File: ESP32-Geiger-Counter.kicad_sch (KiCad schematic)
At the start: 44 parts, among them J1 USB_C_Receptacle_USB2.0_16P, Q1 Q_NPN_BCE, Q2 Q_NPN_BCE, SW1 SW_Push, SW2 SW_Push, U1 TP4056-42-ESOP8, U2 USBLC6-2SC6, U3 ESP32-WROOM-32, U4 TPS63031DSK, U5 Geiger Mueller Tube, U6 CP2102N-Axx-xQFN24

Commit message: basically restarting
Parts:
- removed BT1: Battery_Cell, Connector_JST:JST_PH_B2B-PH-K_1x02_P2.00mm_Vertical, symbol Device:Battery_Cell
- removed C10, C11, C12, C14, C15, C6: 100nF, symbol Device:C
- removed C13, C7, C8: 10uF, symbol Device:C
- removed C16: 100uF, symbol Device:C
- removed C9: 22uF, symbol Device:C
- removed D1: Red LED, symbol Device:LED
- removed D2: Green LED, symbol Device:LED
- removed D3, D4: D_Schottky, symbol Device:D_Schottky
- removed J1: USB_C_Receptacle_USB2.0_16P, symbol Connector:USB_C_Receptacle_USB2.0_16P
- removed Q1, Q2: Q_NPN_BCE, symbol Transistor_BJT:Q_NPN_BCE
- removed R1, R2: 5.1K, symbol Device:R
- removed R10, R11, R5, R9: 10K, symbol Device:R
- removed R3: 22K, symbol Device:R
- removed R4: 2K, symbol Device:R
- removed R6, R7: 1K, symbol Device:R
- removed R8: 47K, symbol Device:R
- removed SW1, SW2: SW_Push, symbol Switch:SW_Push
- removed U1: TP4056-42-ESOP8, Package_SO:SOIC-8-1EP_3.9x4.9mm_P1.27mm_EP2.41x3.3mm_ThermalVias, symbol Battery_Management:TP4056-42-ESOP8
- removed U2: USBLC6-2SC6, Package_TO_SOT_SMD:SOT-23-6, symbol Power_Protection:USBLC6-2SC6
- removed U3: ESP32-WROOM-32, RF_Module:ESP32-WROOM-32, symbol RF_Module:ESP32-WROOM-32
- removed U4: TPS63031DSK, Package_SON:WSON-10-1EP_2.5x2.5mm_P0.5mm_EP1.2x2mm, symbol Regulator_Switching:TPS63031DSK
- removed U5: Geiger Mueller Tube, symbol Custom Parts:Geiger_Mueller_Tube
- removed U6: CP2102N-Axx-xQFN24, Package_DFN_QFN:QFN-24-1EP_4x4mm_P0.5mm_EP2.6x2.6mm, symbol Interface_USB:CP2102N-Axx-xQFN24
- added C1: 1uF, symbol Device:C
- added J1: 2s1p Lipo Battery Pack (8.4V-6V), symbol Connector_Generic:Conn_01x02
- added J2: USB_C_Receptacle_USB2.0_16P, Connector_USB:USB_C_Receptacle_GCT_USB4105-xx-A_16P_TopMnt_Horizontal, symbol Connector:USB_C_Receptacle_USB2.0_16P
- added R1, R2: 5.1K, symbol Device:R_US
- added U1: BQ25886RGE, Package_DFN_QFN:Texas_RGE0024H_VQFN-24-1EP_4x4mm_P0.5mm_EP2.7x2.7mm, symbol Battery_Management:BQ25886RGE
- C2: value 10uF -> 30uF
- C3: value 100nF -> 10uF
- C4: value 10uF -> 47nF
- C5: value 10uF -> 44uF
- F1: value Polyfuse 500mA -> 3A Polyfuse; footprint Fuse:Fuse_1812_4532Metric -> (none)
- L1: value 1.5uH -> 1uH
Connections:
- net +5V: now also F1.1, C1.2, U1.23 (VBUS); no longer C2.1, C3.1, F1.2
- net D+: now also J2.A6 (D+), J2.B6 (D+), U1.24 (D+)
- net D-: now also J2.A7 (D-), J2.B7 (D-), U1.1 (D-)
- net GND: now also C2.1, C3.1, C1.1, J1.1 (Pin_1), J2.A1 (GND), J2.A12 (GND), J2.B1 (GND), J2.B12 (GND), J2.SH (SHIELD), R1.2, R2.1; no longer C2.2, C3.2, C4.1
- net at L1.2: now also C4.1, U1.17 (SW), U1.18 (SW)
- net at L1.1: now also C2.2, C3.2, U1.21 (PMID), U1.22 (PMID)
- net VBAT: no longer names the net of C4.2
- net VBAT: now also U1.12 (BTST)
- net VPWR renamed SYS
- net SYS: now also U1.15 (SYS), U1.16 (SYS)
- new net: F1.2, J2.A4 (VBUS), J2.A9 (VBUS), J2.B4 (VBUS), J2.B9 (VBUS)
- new net: J2.A5 (CC1), R1.1
- new net: J2.B5 (CC2), R2.2
- new net: U1.13 (BAT), U1.14 (BAT)
- new net: U1.19 (GND), U1.20 (GND), U1.25 (GND), U1.4 (GND)
- new net BATT: J1.2 (Pin_2)
- no-connect marks 12 -> 2
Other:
- note added: "Battery Connector"
- note added: "USB Interface"
- note removed: "3.3V Buck Boost Converter"
- note removed: "3.7V Lipo Cell"
- note removed: "Boot/Reset stuff"
- note removed: "Lipo Charging"
- note removed: "Power OR Gate"
- note removed: "USB Input"
- note removed: "USB to ESP"

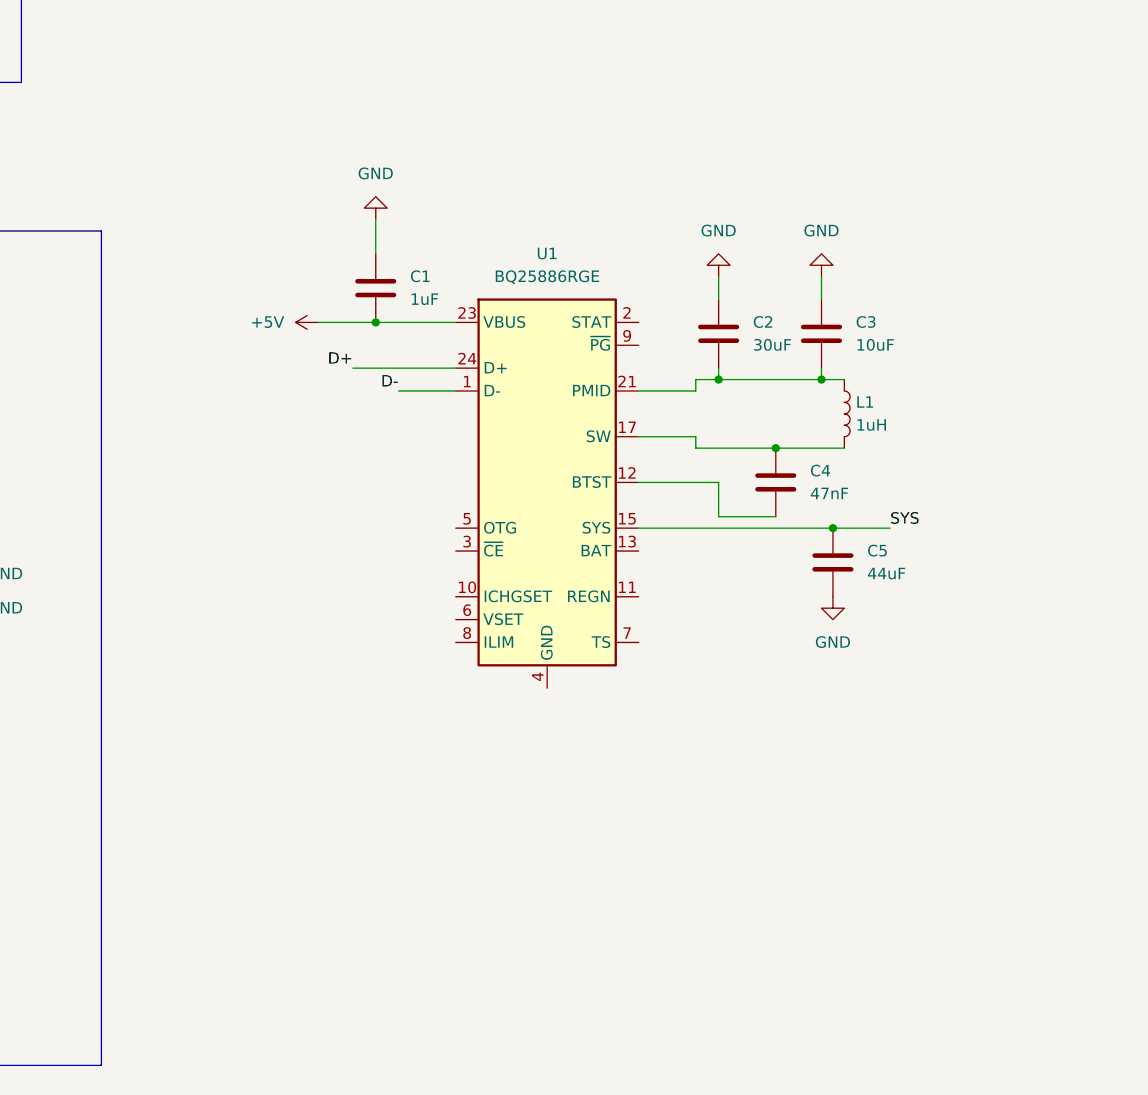
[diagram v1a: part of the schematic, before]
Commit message: added battery charging ic
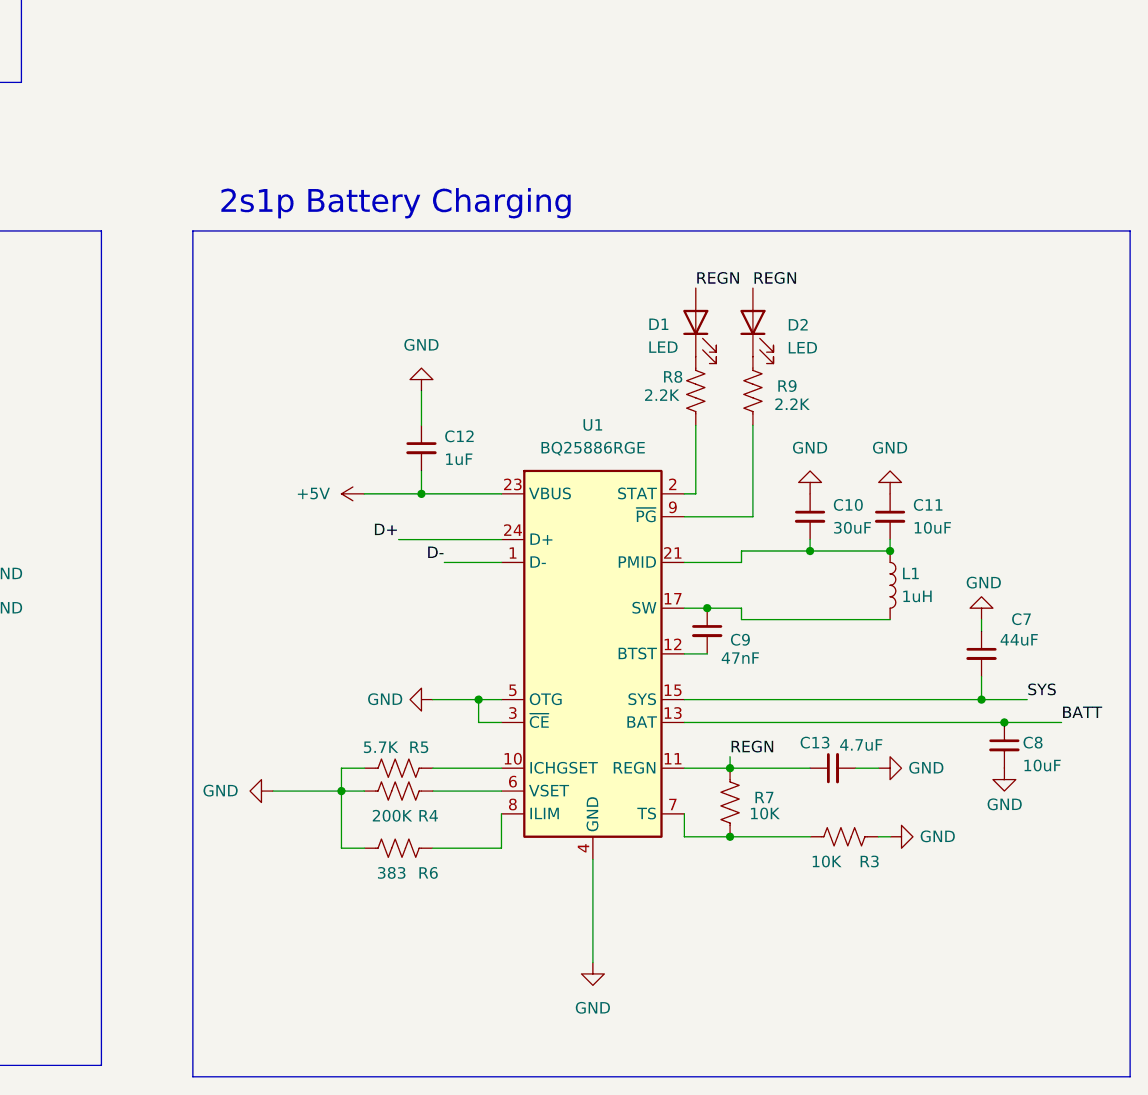
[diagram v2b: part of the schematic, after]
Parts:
- removed C1: 1uF, symbol Device:C
- removed C2: 30uF, symbol Device:C
- removed C3: 10uF, symbol Device:C
- removed C4: 47nF, symbol Device:C
- removed C5: 44uF, symbol Device:C
- added C10: 30uF, symbol Device:C_Small
- added C11, C8: 10uF, symbol Device:C_Small
- added C12: 1uF, symbol Device:C_Small
- added C13: 4.7uF, symbol Device:C_Small
- added C7: 44uF, symbol Device:C_Small
- added C9: 47nF, symbol Device:C_Small
- added D1, D2: LED, symbol Device:LED
- added R3, R7: 10K, symbol Device:R_US
- added R4: 200K, symbol Device:R_US
- added R5: 5.7K, symbol Device:R_US
- added R6: 383, symbol Device:R_US
- added R8, R9: 2.2K, symbol Device:R_US
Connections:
- net +5V: now also C12.2
- net BATT: now also U1.13 (BAT), U1.14 (BAT), C8.1
- net GND: now also U1.19 (GND), U1.20 (GND), U1.25 (GND), U1.3 (~{CE}), U1.4 (GND), U1.5 (OTG), C10.1, C11.1, C12.1, C13.2, C7.1, C8.2, R3.2, R4.1, R5.2, R6.1
- net SYS: now also C7.2
- net at L1.1, U1.21 (PMID), U1.22 (PMID): now also C10.2, C11.2
- net at L1.2, U1.17 (SW), U1.18 (SW): now also C9.1
- net at U1.12 (BTST): now also C9.2
- net at U1.10 (ICHGSET): now also R5.1
- net REGN: now reaches U1.11 (REGN)
- net REGN: now also C13.1, D1.2 (A), D2.2 (A), R7.2
- net at U1.2 (STAT): now also R8.1
- net at U1.6 (VSET): now also R4.2
- net at U1.7 (TS): now also R3.1, R7.1
- net at U1.8 (ILIM): now also R6.2
- net at U1.9 (~{PG}): now also R9.1
- new net: D2.1 (K), R9.2
- new net: D1.1 (K), R8.2
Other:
- note added: "2s1p Battery Charging"
- moved on the sheet: L1, U1

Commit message: big changes, added esp32 wroom 1
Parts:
- added C14, C18, C20: 100nF, symbol Device:C_Small
- added C15, C19: 10uF, symbol Device:C_Small
- added C16, C17: 22uF, symbol Device:C_Small
- added C21: 47uF, symbol Device:C_Small
- added C22: 1uF, symbol Device:C_Small
- added L2: 3.9uH, symbol Device:L
- added R10: 1M, symbol Device:R_US
- added R11: 330k, symbol Device:R_US
- added R12, R13: 10K, symbol Device:R_US
- added SW1: SW_SPDT, symbol Switch:SW_SPDT
- added SW2: RESET, symbol Switch:SW_Push
- added SW3: BOOT, symbol Switch:SW_Push
- added U2: AP63203WU, Package_TO_SOT_SMD:TSOT-23-6, symbol Regulator_Switching:AP63203WU
- added U3: ESP32-S3-WROOM-1, RF_Module:ESP32-S3-WROOM-1, symbol RF_Module:ESP32-S3-WROOM-1
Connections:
- net D+: now also U3.14 (USB_D+)
- net D-: now also U3.13 (USB_D-)
- net GND: now also C15.2, C16.2, C17.2, C18.2, C19.2, C20.2, C21.2, C22.2, R11.1, SW2.2, SW3.1, U2.4 (GND), U3.1 (GND), U3.40 (GND), U3.41 (GND)
- net SYS: now also SW1.2 (B)
- new net: R13.2, SW3.2, U3.27 (IO0)
- new net: C22.1, R12.1, SW2.1, U3.3 (EN)
- new net: C14.1, L2.1, U2.5 (SW)
- new net: C14.2, U2.6 (BST)
- new net +3.3V: C16.1, C17.1, C19.1, C20.1, C21.1, L2.2, R12.2, R13.1, U2.1 (FB), U3.2 (3V3)
- new net VBAT_SENSE: C18.1, R10.1, R11.2
- new net VSYS_SW: C15.1, R10.2, SW1.1 (A), U2.2 (EN), U2.3 (IN)
- no-connect marks 2 -> 3
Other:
- note added: "3.3V Buck Converter"
- note added: "Battery Voltage to ESP32"
- note added: "Main on/off switch"

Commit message: working on HV boost
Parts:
- added C23: 10uF 25V, symbol Device:C_Small
- added C24, C25, C27: 10nF 1kV, symbol Device:C_Small
- added C26: 10nF, symbol Device:C_Small
- added D3: 1000V, symbol Device:D
- added D4, D5, D6: 150V Zener, symbol Device:D_Zener
- added J3: SBM20 +, symbol Connector_Generic:Conn_01x01
- added J4: SBM20 -, symbol Connector_Generic:Conn_01x01
- added L3: 10mH, symbol Device:L
- added Q1: NMOS, symbol Simulation_SPICE:NMOS
- added Q2: 2N3904, Package_TO_SOT_THT:TO-92_Inline, symbol Transistor_BJT:2N3904
- added R14, R15, R16: 100M, symbol Device:R_US
- added R17: 680k, symbol Device:R_US
- added R18: 1M, symbol Device:R_US
- added R19: 5.1M, symbol Device:R_US
- added R20: 100k, symbol Device:R_US
- added R21, R22: 10k, symbol Device:R_US
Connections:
- net +3.3V: now also R22.1
- net GND: now also C23.2, C24.2, C25.2, C26.2, C27.2, D6.2 (A), Q1.3 (S), Q2.1 (E), R17.1, R20.1
- net VSYS_SW: now also C23.1, L3.1
- new net: J4.1 (Pin_1), R20.2, R21.1
- new net: C24.1, C25.1, D3.1 (K), D4.1 (K), R14.2, R18.1
- new net: D3.2 (A), L3.2, Q1.1 (D)
- new net: R15.1, R16.2
- new net: R14.1, R15.2
- new net: D4.2 (A), D5.1 (K)
- new net: D5.2 (A), D6.1 (K)
- new net: C27.1, R18.2, R19.1
- new net: J3.1 (Pin_1), R19.2
- new net: Q2.2 (B), R21.2
- new net HV_SENSE: C26.1, R16.1, R17.2
- new net PULSE: Q2.3 (C), R22.2

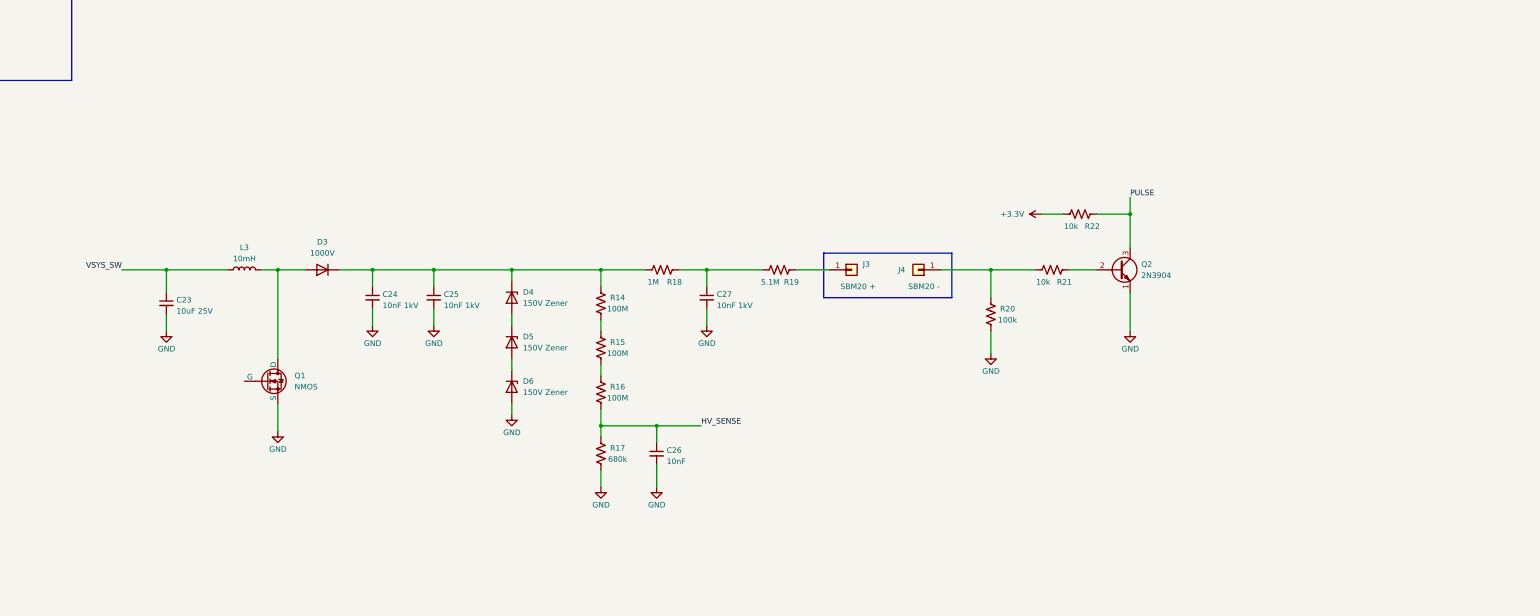
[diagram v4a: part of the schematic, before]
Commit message: finished working 400v boost and tube topo
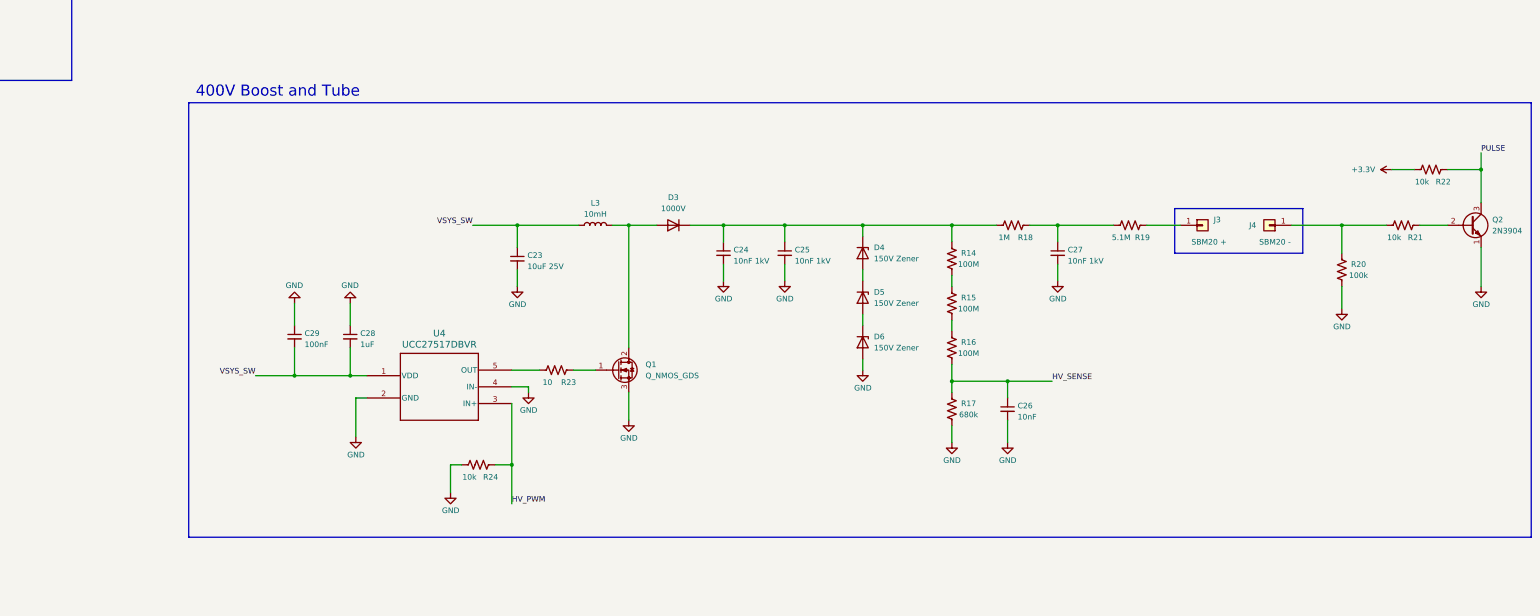
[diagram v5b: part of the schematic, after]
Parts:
- removed Q1: NMOS, symbol Simulation_SPICE:NMOS
- added C28: 1uF, symbol Device:C_Small
- added C29: 100nF, symbol Device:C_Small
- added Q1: Q_NMOS_GDS, Package_TO_SOT_SMD:SOT-223-3_TabPin2, symbol Transistor_FET:Q_NMOS_GDS
- added R23: 10, symbol Device:R_US
- added R24: 10k, symbol Device:R_US
- added U4: UCC27517DBVR, footprints:DBV5_TEX, symbol UCC27517:UCC27517DBVR
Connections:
- net GND: now also C28.1, C29.1, Q1.3 (S), R24.1, U4.2 (GND), U4.4 (IN-)
- net VSYS_SW: now also C28.2, C29.2, U4.1 (VDD)
- net at D3.2 (A), L3.2: now also Q1.2 (D)
- new net: Q1.1 (G), R23.2
- new net: R23.1, U4.5 (OUT)
- new net HV_PWM: R24.2, U4.3 (IN+)
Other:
- note added: "400V Boost and Tube"
- moved on the sheet: C23, C24, C25, C26, C27, D3, D4, D5, D6, J3, J4, L3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

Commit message: esp32 work
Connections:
- net HV_PWM: now also U3.4 (IO4)
- net HV_SENSE: now also U3.38 (IO2)
- net PULSE: now also U3.5 (IO5)
- net VBAT_SENSE: now also U3.39 (IO1)
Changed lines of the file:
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@@
+	(wire
+		(pts
+			(xy 142.24 232.41) (xy 148.59 232.41)
+		)
+		(stroke
+			(width 0)
+			(type default)
+		)
+	)
 	(wire
 		(pts
@@
 	(wire
 		(pts
+			(xy 142.24 240.03) (xy 148.59 240.03)
+		)
+		(stroke
+			(width 0)
+			(type default)
+		)
+	)
+	(wire
+		(pts
 			(xy 447.04 199.39) (xy 447.04 203.2)
 		)
@@
 	(wire
 		(pts
+			(xy 143.51 229.87) (xy 148.59 229.87)
+		)
+		(stroke
+			(width 0)
+			(type default)
+		)
+	)
+	(wire
+		(pts
 			(xy 303.53 123.19) (xy 283.21 123.19)
 		)
@@
 	(wire
 		(pts
+			(xy 142.24 237.49) (xy 148.59 237.49)
+		)
+		(stroke
+			(width 0)
+			(type default)
+		)
+	)
+	(wire
+		(pts
 			(xy 435.61 243.84) (xy 435.61 248.92)
 		)
@@
 			(width 0)
 			(type default)
+		)
+	)
+	(label "PULSE"
+		(at 142.24 240.03 180)
+		(effects
+			(font
+				(size 1.27 1.27)
+			)
+			(justify right bottom)
 		)
 	)
@@
 		)
 	)
+	(label "HV_SENSE"
+		(at 142.24 232.41 180)
+		(effects
+			(font
+				(size 1.27 1.27)
+			)
+			(justify right bottom)
+		)
+	)
 	(label "D-"
 		(at 182.88 232.41 0)
@@
 		)
 	)
+	(label "HV_PWM"
+		(at 142.24 237.49 180)
+		(effects
+			(font
+				(size 1.27 1.27)
+			)
+			(justify right bottom)
+		)
+	)
 	(label "BATT"
 		(at 80.01 44.45 0)
@@
 		)
 	)
+	(label "VBAT_SENSE"
+		(at 143.51 229.87 180)
+		(effects
+			(font
+				(size 1.27 1.27)
+			)
+			(justify right bottom)
+		)
+	)

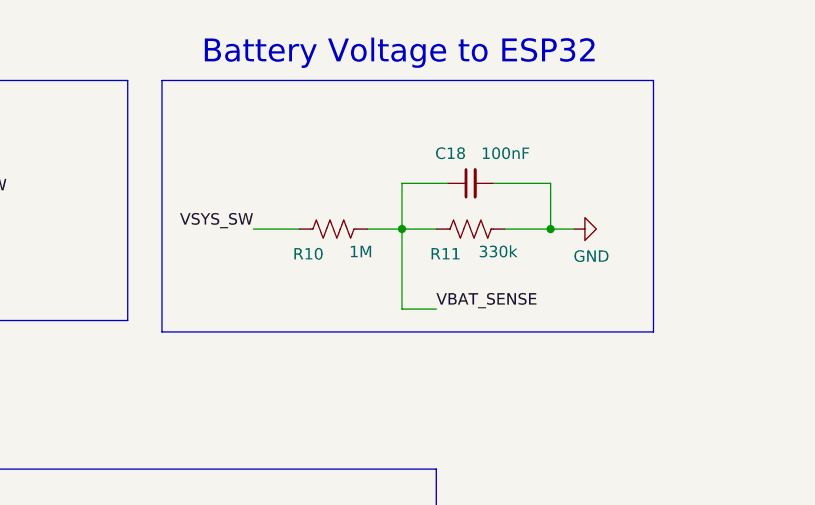
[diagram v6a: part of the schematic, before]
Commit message: footprint changes
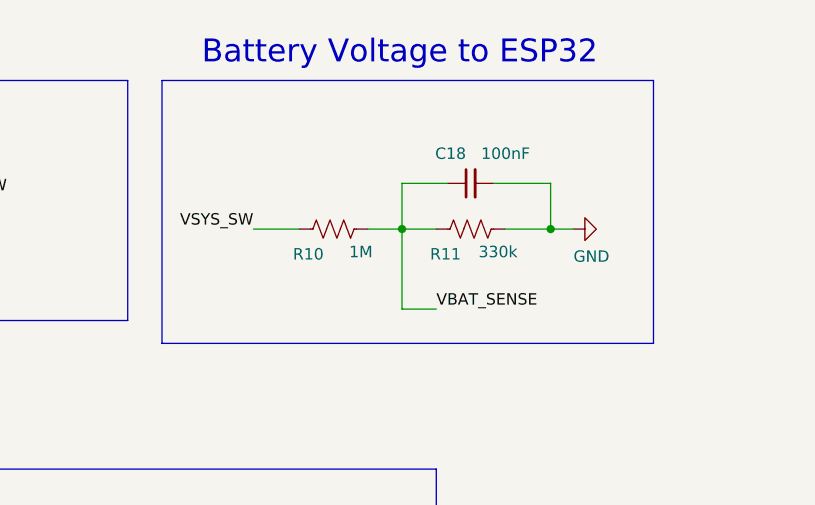
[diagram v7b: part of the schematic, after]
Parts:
- U1: footprint Package_DFN_QFN:Texas_RGE0024H_VQFN-24-1EP_4x4mm_P0.5mm_EP2.7x2.7mm -> Package_DFN_QFN:Texas_RGE0024H_VQFN-24-1EP_4x4mm_P0.5mm_EP2.7x2.7mm_ThermalVias
- U2: footprint Package_TO_SOT_SMD:TSOT-23-6 -> Package_TO_SOT_SMD:TSOT-23-6_HandSoldering
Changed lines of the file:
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@@
 	(rectangle
 		(start 191.77 29.21)
-		(end 246.38 57.15)
+		(end 246.38 58.42)
 		(stroke
 			(width 0)
@@
 			)
 		)
-		(property "Footprint" "Package_TO_SOT_SMD:TSOT-23-6"
+		(property "Footprint" "Package_TO_SOT_SMD:TSOT-23-6_HandSoldering"
 			(at 273.05 143.51 0)
 			(hide yes)
@@
 			)
 		)
-		(property "Footprint" "Package_DFN_QFN:Texas_RGE0024H_VQFN-24-1EP_4x4mm_P0.5mm_EP2.7x2.7mm"
+		(property "Footprint" "Package_DFN_QFN:Texas_RGE0024H_VQFN-24-1EP_4x4mm_P0.5mm_EP2.7x2.7mm_ThermalVias"
 			(at 162.56 148.844 0)
 			(hide yes)
